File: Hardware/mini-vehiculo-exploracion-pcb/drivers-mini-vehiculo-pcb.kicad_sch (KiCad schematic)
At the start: 30 parts, among them J1 Conn_01x08_Pin_drv, J2 Conn_01x02_Pin_drv, J3 Conn_01x03_Pin, J4 Conn_01x02_Motor1, J5 Conn_01x02_Motor2, J6 Battery_Terminal_01x02, U1 DRV8873HPWPRQ1, U2 DRV8873HPWPRQ1

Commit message: updated drv pcb
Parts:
- removed J3: Conn_01x03_Pin, Connector_PinSocket_2.54mm:PinSocket_1x03_P2.54mm_Vertical, symbol Connector:Conn_01x03_Pin
- removed J4: Conn_01x02_Motor1, Connector_PinSocket_2.54mm:PinSocket_1x02_P2.54mm_Vertical, symbol Connector:Conn_01x02_Pin
- removed J5: Conn_01x02_Motor2, Connector_PinSocket_2.54mm:PinSocket_1x02_P2.54mm_Vertical, symbol Connector:Conn_01x02_Pin
- added J4: Motor1_Terminal, TerminalBlock_Phoenix:TerminalBlock_Phoenix_MPT-0,5-2-2.54_1x02_P2.54mm_Horizontal, symbol Connector:Screw_Terminal_01x02
- added J5: Motor2_Terminal, TerminalBlock_Phoenix:TerminalBlock_Phoenix_MPT-0,5-2-2.54_1x02_P2.54mm_Horizontal, symbol Connector:Screw_Terminal_01x02
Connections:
- net GND: now also U1.25 (EXP), U1.P1 (EXP), U1.P10 (EXP), U1.P11 (EXP), U1.P12 (EXP), U1.P13 (EXP), U1.P14 (EXP), U1.P15 (EXP), U1.P16 (EXP), U1.P17 (EXP), U1.P18 (EXP), U1.P2 (EXP), U1.P3 (EXP), U1.P4 (EXP), U1.P5 (EXP), U1.P6 (EXP), U1.P7 (EXP), U1.P8 (EXP), U1.P9 (EXP), U2.25 (EXP), U2.P1 (EXP), U2.P10 (EXP), U2.P11 (EXP), U2.P12 (EXP), U2.P13 (EXP), U2.P14 (EXP), U2.P15 (EXP), U2.P16 (EXP), U2.P17 (EXP), U2.P18 (EXP), U2.P2 (EXP), U2.P3 (EXP), U2.P4 (EXP), U2.P5 (EXP), U2.P6 (EXP), U2.P7 (EXP), U2.P8 (EXP), U2.P9 (EXP)
- net M1_V+: now also J4.2 (Pin_2)
- net M1_V-: now also J4.1 (Pin_1)
- net M2_V+: now also J5.2 (Pin_2)
- net M2_V-: now also J5.1 (Pin_1)
- net SERVO_CRL: no longer names the net of J1.4 (Pin_4)
- no-connect marks 4 -> 3
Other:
- note added: "IO38"
- note removed: "IO39"
- note removed: "TO SERVOMOTOR"

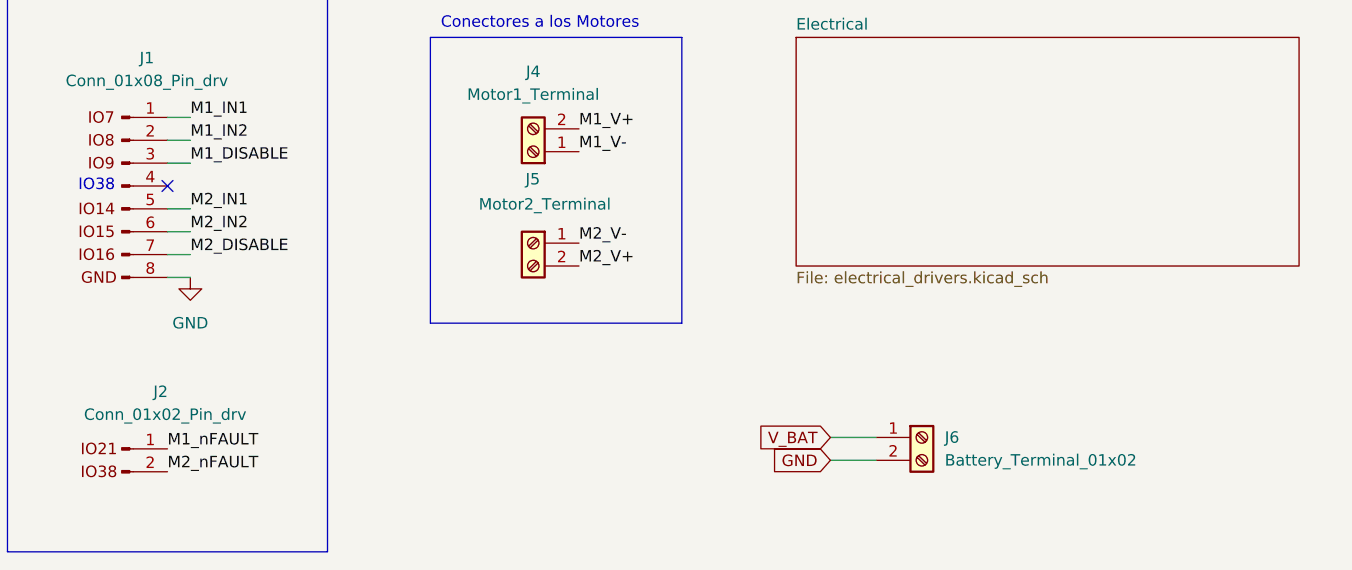
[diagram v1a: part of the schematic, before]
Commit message: updated gnd and 12v zones
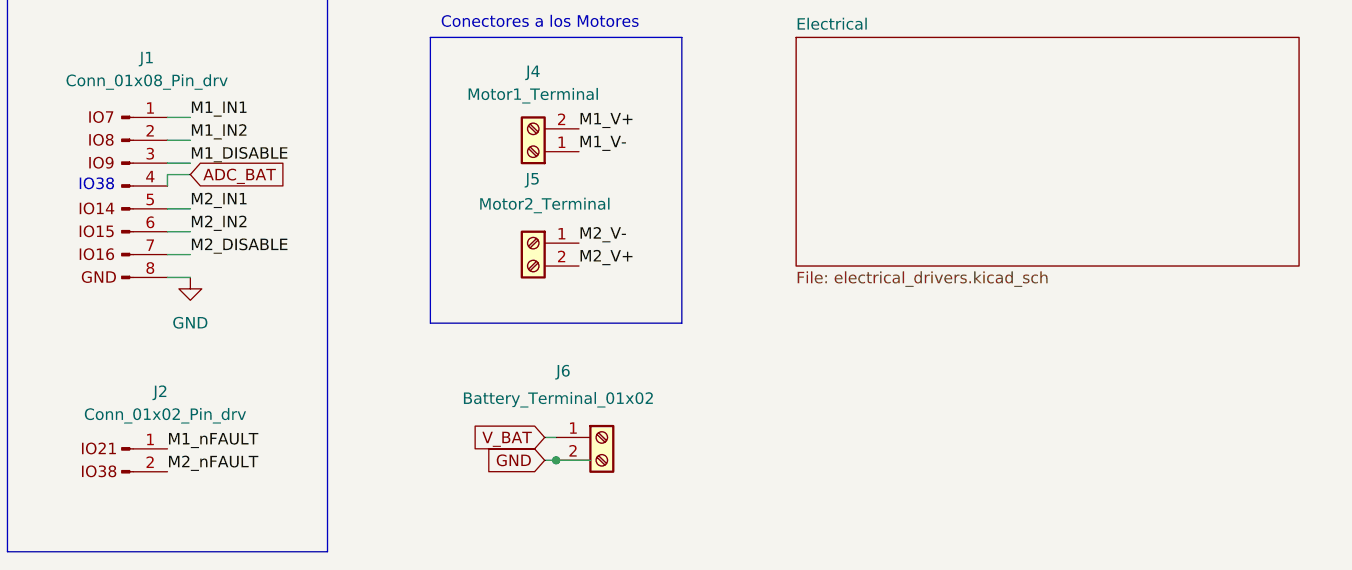
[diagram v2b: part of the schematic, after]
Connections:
- net ADC_BAT: now reaches J1.4 (Pin_4)
- no-connect marks 3 -> 2
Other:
- moved on the sheet: J6
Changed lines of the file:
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@@
 	)
 	(junction
+		(at 90.17 176.53)
+		(diameter 0)
+		(color 0 0 0 0)
+	)
+	(junction
 		(at 54.61 64.77)
 		(diameter 0)
@@
 		(at 222.25 99.06)
 	)
-	(no_connect
-		(at 46.99 146.05)
-	)
 	(wire
 		(pts
@@
 	(wire
 		(pts
-			(xy 120.65 173.99) (xy 125.73 173.99)
+			(xy 88.9 173.99) (xy 90.17 173.99)
 		)
 		(stroke
@@
 	(wire
 		(pts
+			(xy 46.99 144.78) (xy 46.99 146.05)
+		)
+		(stroke
+			(width 0)
+			(type default)
+		)
+	)
+	(wire
+		(pts
 			(xy 110.49 87.63) (xy 118.11 87.63)
 		)
@@
 	(wire
 		(pts
+			(xy 93.98 176.53) (xy 90.17 176.53)
+		)
+		(stroke
+			(width 0)
+			(type default)
+		)
+	)
+	(wire
+		(pts
 			(xy 181.61 41.91) (xy 184.15 41.91)
 		)
@@
 	(wire
 		(pts
-			(xy 120.65 176.53) (xy 125.73 176.53)
+			(xy 88.9 176.53) (xy 90.17 176.53)
 		)
 		(stroke
@@
 	(wire
 		(pts
+			(xy 49.53 144.78) (xy 46.99 144.78)
+		)
+		(stroke
+			(width 0)
+			(type default)
+		)
+	)
+	(wire
+		(pts
 			(xy 156.21 66.04) (xy 166.37 66.04)
 		)
@@
 	(global_label "V_BAT"
 		(shape input)
-		(at 120.65 173.99 180)
+		(at 88.9 173.99 180)
 		(fields_autoplaced yes)
 		(effects
@@
 		)
 		(property "Intersheetrefs" "${INTERSHEET_REFS}"
-			(at 112.2824 173.99 0)
+			(at 80.5324 173.99 0)
 			(effects
 				(font
@@
 		)
 	)
+	(global_label "ADC_BAT"
+		(shape input)
+		(at 49.53 144.78 0)
+		(fields_autoplaced yes)
+		(effects
+			(font
+				(size 1.27 1.27)
+			)
+			(justify left)
+		)
+		(property "Intersheetrefs" "${INTERSHEET_REFS}"
+			(at 60.4376 144.78 0)
+			(effects
+				(font
+					(size 1.27 1.27)
+				)
+				(justify left)
+				(hide yes)
+			)
+		)
+	)
 	(global_label "DVDD_2"
 		(shape input)
@@
 	(global_label "GND"
 		(shape input)
-		(at 120.65 176.53 180)
+		(at 88.9 176.53 180)
 		(fields_autoplaced yes)
 		(effects
@@
 		)
 		(property "Intersheetrefs" "${INTERSHEET_REFS}"
-			(at 113.7943 176.53 0)
+			(at 82.0443 176.53 0)
 			(effects
 				(font
@@
 	(symbol
 		(lib_id "Connector:Screw_Terminal_01x02")
-		(at 130.81 173.99 0)
+		(at 95.25 173.99 0)
 		(unit 1)
 		(exclude_from_sim no)
@@
 		(on_board yes)
 		(dnp no)
-		(fields_autoplaced yes)
 		(property "Reference" "J6"
-			(at 133.35 173.9899 0)
+			(at 90.17 166.624 0)
 			(effects
 				(font
@@
 		)
 		(property "Value" "Battery_Terminal_01x02"
-			(at 133.35 176.5299 0)
+			(at 79.756 169.672 0)
 			(effects
 				(font
@@
 		)
 		(property "Footprint" "TerminalBlock_Phoenix:TerminalBlock_Phoenix_MPT-0,5-2-2.54_1x02_P2.54mm_Horizontal"
-			(at 130.81 173.99 0)
+			(at 95.25 173.99 0)
 			(effects
 				(font
@@
 		)
 		(property "Datasheet" "~"
-			(at 130.81 173.99 0)
+			(at 95.25 173.99 0)
 			(effects
 				(font
@@
 		)
 		(property "Description" "Generic screw terminal, single row, 01x02, script generated (kicad-library-utils/schlib/autogen/connector/)"
-			(at 130.81 173.99 0)
+			(at 95.25 173.99 0)
 			(effects
 				(font
